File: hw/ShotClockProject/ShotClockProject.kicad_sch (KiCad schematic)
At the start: 8 parts, among them SW1 PS-5824SVB-6PL

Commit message: Finshed both schematics
- LED driving transistors are placed
- All connectors on segment display PCB are placed
- All schematic references have been re-configured (autosort on Y axis)
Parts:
- renumbered R39 to R3, R40 to R4, TP2 to TP1, TP1 to TP2, TP12 to TP3
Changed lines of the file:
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@@
   (symbol (lib_id "Connector:TestPoint") (at 144.78 54.61 0) (mirror y) (unit 1)
     (in_bom yes) (on_board yes) (dnp no)
-    (property "Reference" "TP12" (at 143.51 49.53 0)
+    (property "Reference" "TP3" (at 143.51 49.53 0)
       (effects (font (size 1.27 1.27)) (justify left))
     )
@@
       (project "ShotClockProject"
         (path "/5fd859aa-754d-49c2-9762-3f7ebe3bb64c"
-          (reference "TP12") (unit 1)
+          (reference "TP3") (unit 1)
         )
         (path "/5fd859aa-754d-49c2-9762-3f7ebe3bb64c/17367eb9-0f4d-4017-b1ca-d50430410a5d"
@@
         )
         (path "/5fd859aa-754d-49c2-9762-3f7ebe3bb64c"
-          (reference "#FLG013") (unit 1)
+          (reference "#FLG02") (unit 1)
         )
       )
@@
   (symbol (lib_id "Connector:TestPoint") (at 144.78 35.56 0) (mirror y) (unit 1)
     (in_bom yes) (on_board yes) (dnp no)
-    (property "Reference" "TP2" (at 143.51 30.48 0)
+    (property "Reference" "TP1" (at 143.51 30.48 0)
       (effects (font (size 1.27 1.27)) (justify left))
     )
@@
       (project "ShotClockProject"
         (path "/5fd859aa-754d-49c2-9762-3f7ebe3bb64c"
-          (reference "TP2") (unit 1)
+          (reference "TP1") (unit 1)
         )
         (path "/5fd859aa-754d-49c2-9762-3f7ebe3bb64c/17367eb9-0f4d-4017-b1ca-d50430410a5d"
@@
   (symbol (lib_id "power:+5V") (at 160.02 53.34 0) (unit 1)
     (in_bom yes) (on_board yes) (dnp no) (fields_autoplaced)
-    (property "Reference" "#PWR089" (at 160.02 57.15 0)
+    (property "Reference" "#PWR02" (at 160.02 57.15 0)
       (effects (font (size 1.27 1.27)) hide)
     )
@@
       (project "ShotClockProject"
         (path "/5fd859aa-754d-49c2-9762-3f7ebe3bb64c"
-          (reference "#PWR089") (unit 1)
+          (reference "#PWR02") (unit 1)
         )
       )
@@
   (symbol (lib_id "Device:R") (at 149.86 54.61 90) (unit 1)
     (in_bom yes) (on_board yes) (dnp no) (fields_autoplaced)
-    (property "Reference" "R40" (at 149.86 48.26 90)
+    (property "Reference" "R4" (at 149.86 48.26 90)
       (effects (font (size 1.27 1.27)))
     )
@@
       (project "ShotClockProject"
         (path "/5fd859aa-754d-49c2-9762-3f7ebe3bb64c"
-          (reference "R40") (unit 1)
+          (reference "R4") (unit 1)
         )
       )
@@
   (symbol (lib_id "Connector:TestPoint") (at 59.69 49.53 0) (mirror y) (unit 1)
     (in_bom yes) (on_board yes) (dnp no)
-    (property "Reference" "TP1" (at 58.42 45.72 0)
+    (property "Reference" "TP2" (at 58.42 45.72 0)
       (effects (font (size 1.27 1.27)) (justify left))
     )
@@
       (project "ShotClockProject"
         (path "/5fd859aa-754d-49c2-9762-3f7ebe3bb64c"
-          (reference "TP1") (unit 1)
+          (reference "TP2") (unit 1)
         )
         (path "/5fd859aa-754d-49c2-9762-3f7ebe3bb64c/d287d155-1951-4d4f-8d6c-570f03bc79f5"
@@
   (symbol (lib_id "Device:R") (at 101.6 54.61 90) (unit 1)
     (in_bom yes) (on_board yes) (dnp no) (fields_autoplaced)
-    (property "Reference" "R39" (at 101.6 48.26 90)
+    (property "Reference" "R3" (at 101.6 48.26 90)
       (effects (font (size 1.27 1.27)))
     )
@@
       (project "ShotClockProject"
         (path "/5fd859aa-754d-49c2-9762-3f7ebe3bb64c"
-          (reference "R39") (unit 1)
-        )
-      )
+          (reference "R3") (unit 1)
+        )
+      )

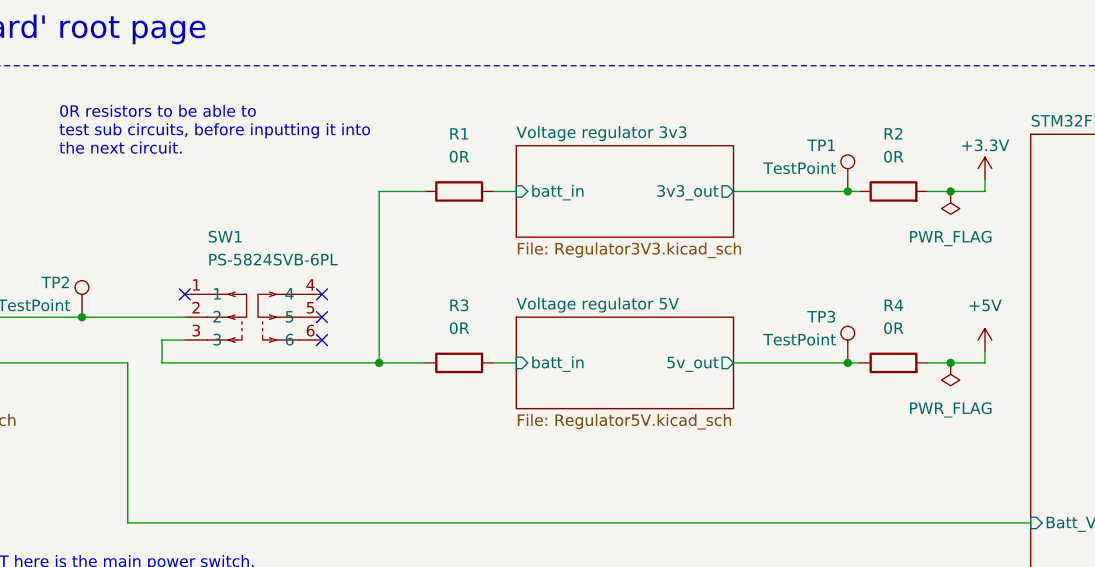
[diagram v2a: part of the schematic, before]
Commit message: Redid layout with new board dimensions
Changed tactile switches to larger push switches (also momentary)
Changed USART1 to UART4 & added UART5 to STDC14 connector
Placed all components nearer to each other, and within the PCB outer edge
Added rounded corners
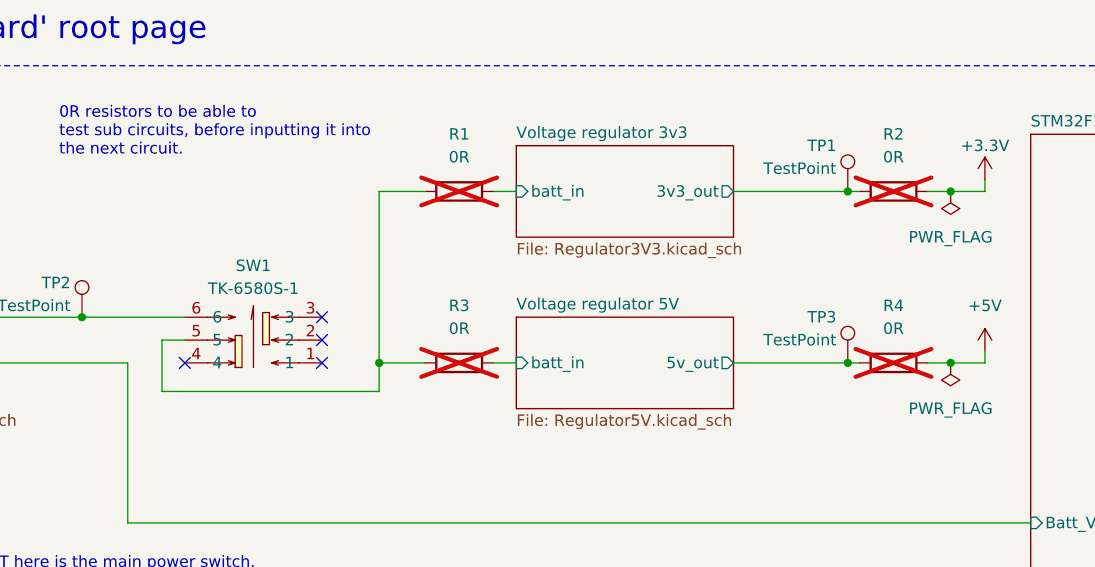
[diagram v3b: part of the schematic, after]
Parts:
- removed SW1: PS-5824SVB-6PL, PS-5824SVB-6PL:SW-SMD_6P-L5.8-W5.8-P2.00-LS11.3, symbol PS-5824SVB-6PL:PS-5824SVB-6PL
- added SW1: TK-6580S-1, TK-6580S-1:SW-SMD_TK-6580S-1, symbol TK-6580S-1:TK-6580S-1
- R1, R2, R3, R4: now not fitted
- TP1, TP2, TP3: footprint TestPoint:TestPoint_Pad_D2.5mm -> TestPoint:TestPoint_Pad_D1.0mm
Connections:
- net Li-Po Battery and charger/charger_out: now also SW1.6
- net at R1.1, R3.1: now also SW1.5

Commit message: Routed almost everything, except display connector
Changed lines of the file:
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@@
   (no_connect (at 86.36 52.07))
   (no_connect (at 86.36 49.53))
+  (bus_entry (at 118.745 120.015) (size 2.54 2.54)
+    (stroke (width 0) (type default))
+  )
   (wire (pts (xy 203.2 45.72) (xy 231.14 45.72))
     (stroke (width 0) (type default))

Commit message: Added LCSC Part number
Renamed output folders
Created first output files for REV1
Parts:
- R1, R2, R3, R4: LCSC Part (none) -> C17168; LCSC Part # (none) -> C17168
- SW1: LCSC Part # (none) -> C528774
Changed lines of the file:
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@@
       (effects (font (size 1.27 1.27)) hide)
     )
-    (property "LCSC Part" "C528774" (at 96.52 52.07 0)
+    (property "LCSC Part #" "C528774" (at 78.74 52.07 0)
+      (effects (font (size 1.27 1.27)) hide)
+    )
+    (property "LCSC Part" "C528774" (at 78.74 52.07 0)
       (effects (font (size 1.27 1.27)) hide)
     )
@@
       (effects (font (size 1.27 1.27)) hide)
     )
+    (property "LCSC Part #" "" (at 144.78 54.61 0)
+      (effects (font (size 1.27 1.27)) hide)
+    )
+    (property "LCSC Part" "" (at 144.78 54.61 0)
+      (effects (font (size 1.27 1.27)) hide)
+    )
     (pin "1")
     (instances
@@
       (effects (font (size 1.27 1.27)) hide)
     )
+    (property "LCSC Part #" "" (at 144.78 35.56 0)
+      (effects (font (size 1.27 1.27)) hide)
+    )
+    (property "LCSC Part" "" (at 144.78 35.56 0)
+      (effects (font (size 1.27 1.27)) hide)
+    )
     (pin "1")
     (instances
@@
       (effects (font (size 1.27 1.27)) hide)
     )
+    (property "LCSC Part #" "C17168" (at 149.86 35.56 0)
+      (effects (font (size 1.27 1.27)) hide)
+    )
+    (property "LCSC Part" "C17168" (at 149.86 35.56 0)
+      (effects (font (size 1.27 1.27)) hide)
+    )
     (pin "1")
     (pin "2")
@@
       (effects (font (size 1.27 1.27)) hide)
     )
+    (property "LCSC Part #" "C17168" (at 101.6 35.56 0)
+      (effects (font (size 1.27 1.27)) hide)
+    )
+    (property "LCSC Part" "C17168" (at 101.6 35.56 0)
+      (effects (font (size 1.27 1.27)) hide)
+    )
     (pin "1")
     (pin "2")
@@
       (effects (font (size 1.27 1.27)) hide)
     )
+    (property "LCSC Part #" "C17168" (at 149.86 54.61 0)
+      (effects (font (size 1.27 1.27)) hide)
+    )
+    (property "LCSC Part" "C17168" (at 149.86 54.61 0)
+      (effects (font (size 1.27 1.27)) hide)
+    )
     (pin "1")
     (pin "2")
@@
       (effects (font (size 1.27 1.27)) hide)
     )
+    (property "LCSC Part #" "" (at 59.69 49.53 0)
+      (effects (font (size 1.27 1.27)) hide)
+    )
+    (property "LCSC Part" "" (at 59.69 49.53 0)
+      (effects (font (size 1.27 1.27)) hide)
+    )
     (pin "1")
     (instances
@@
       (effects (font (size 1.27 1.27)) hide)
     )
+    (property "LCSC Part #" "C17168" (at 101.6 54.61 0)
+      (effects (font (size 1.27 1.27)) hide)
+    )
+    (property "LCSC Part" "C17168" (at 101.6 54.61 0)
+      (effects (font (size 1.27 1.27)) hide)
+    )

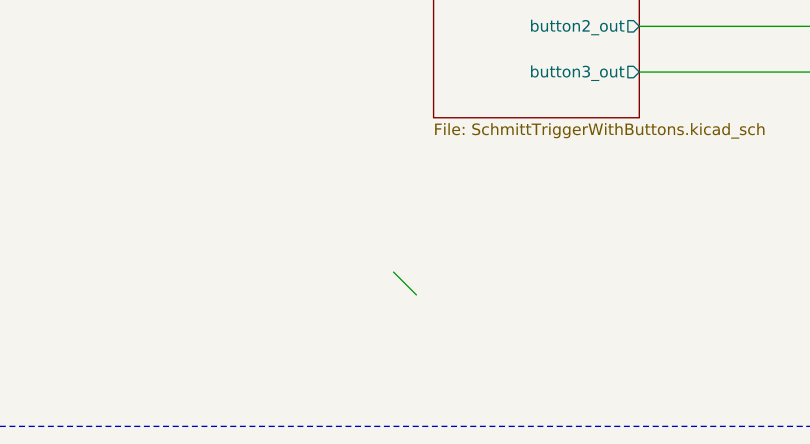
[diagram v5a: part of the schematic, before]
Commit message: Added LCSC part numbers, and changed TPS vias
- Changed the footprint for the TPS regulators, so they don't have 0.2mm vias. Manually placed GND vias next to the footprint.
- Removed NETTIES to get rid of weird across the map connection of GND and GNDPWR.
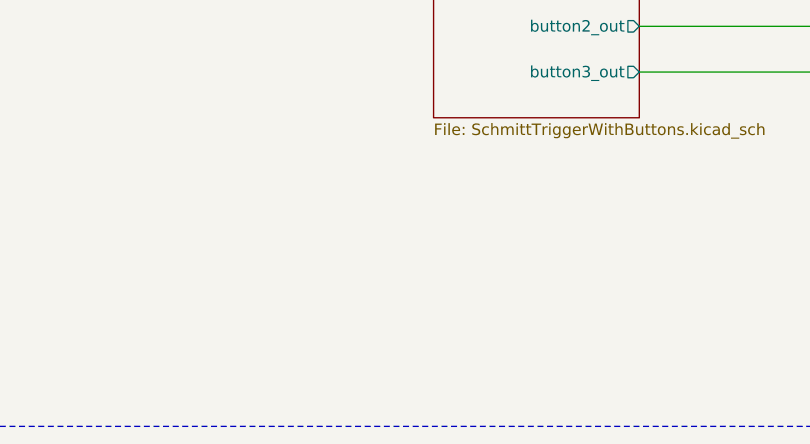
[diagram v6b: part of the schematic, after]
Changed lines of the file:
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@@
   (no_connect (at 86.36 52.07))
   (no_connect (at 86.36 49.53))
-  (bus_entry (at 118.745 120.015) (size 2.54 2.54)
-    (stroke (width 0) (type default))
-  )
   (wire (pts (xy 203.2 45.72) (xy 231.14 45.72))
     (stroke (width 0) (type default))

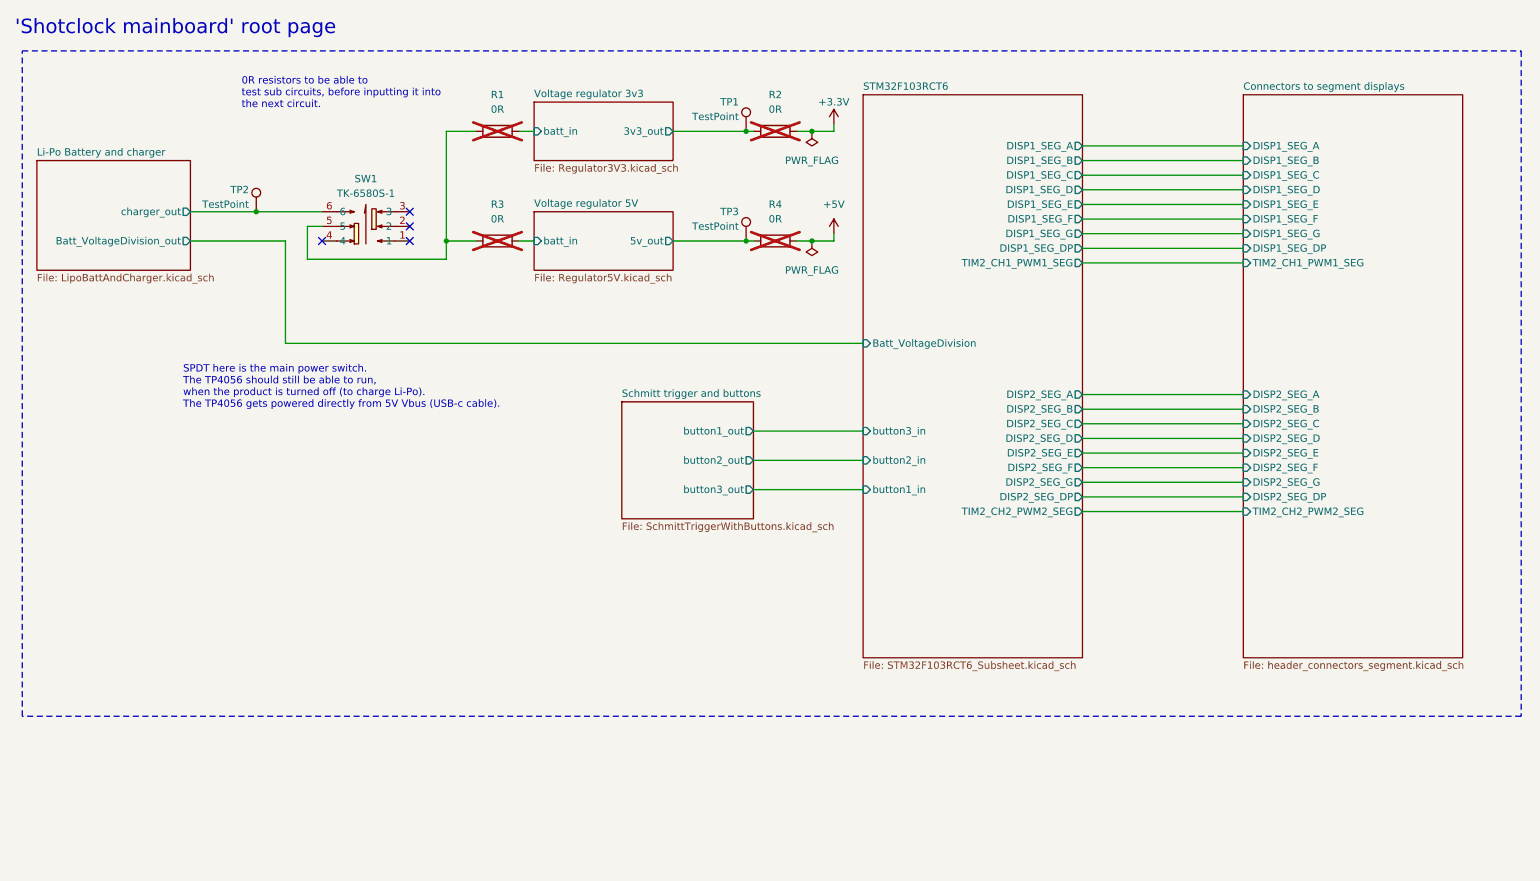
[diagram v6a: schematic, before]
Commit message: Started on integrating new STM32 MCU
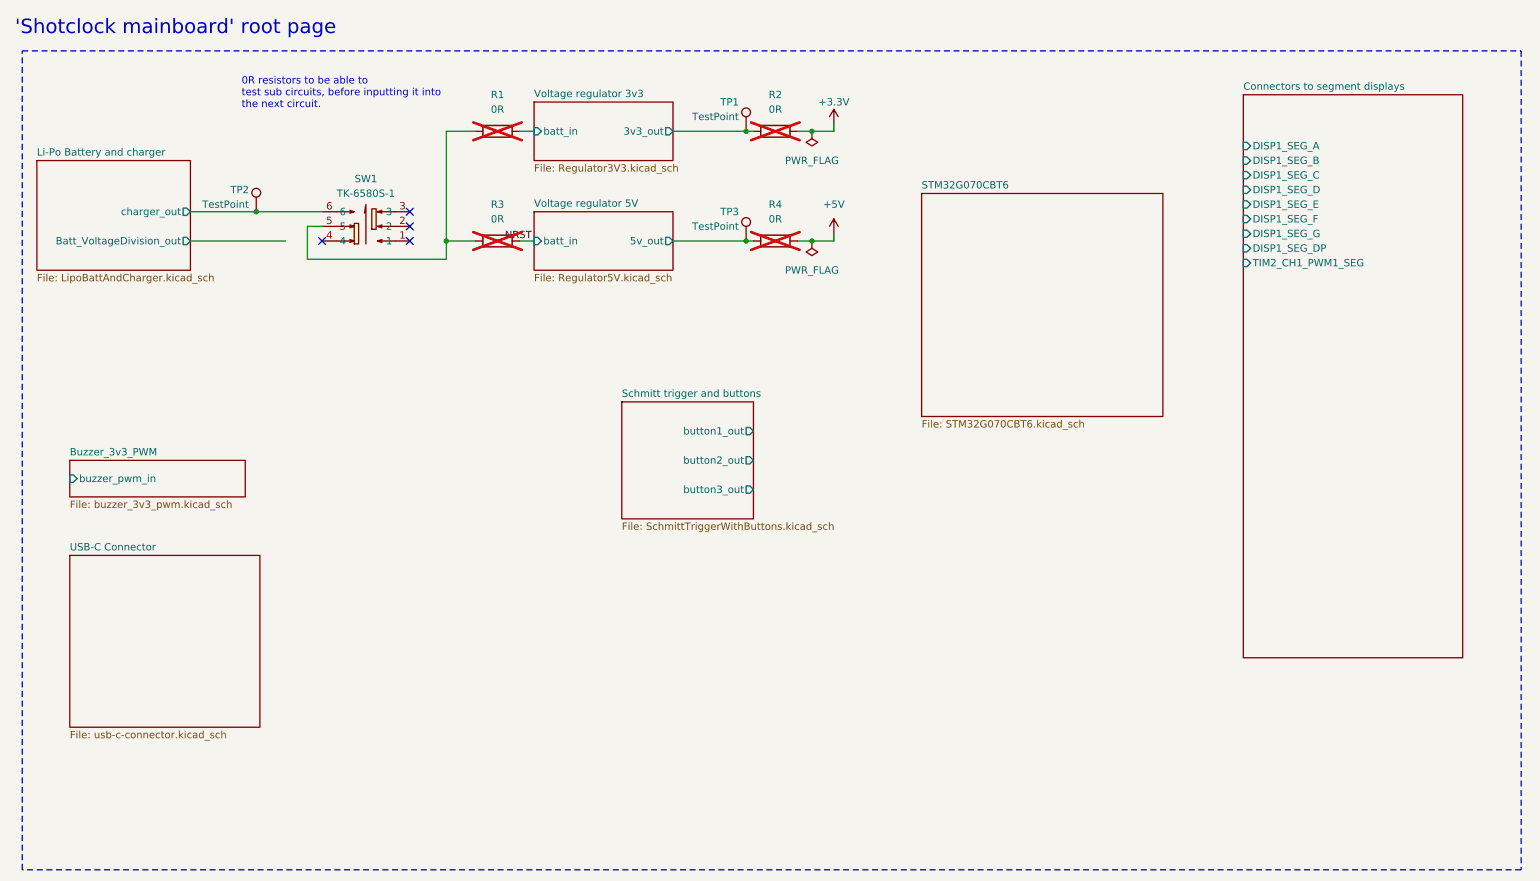
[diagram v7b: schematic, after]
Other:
- removed sheet STM32F103RCT6
- added sheet Buzzer_3v3_PWM (buzzer_3v3_pwm.kicad_sch)
- added sheet STM32G070CBT6 (STM32G070CBT6.kicad_sch)
- added sheet USB-C Connector (usb-c-connector.kicad_sch)
- sheet Connectors to segment displays ports: added none; removed DISP2_SEG_A, DISP2_SEG_B, DISP2_SEG_C, DISP2_SEG_D, DISP2_SEG_DP, DISP2_SEG_E, DISP2_SEG_F, DISP2_SEG_G, TIM2_CH2_PWM2_SEG
- note removed: "SPDT here is the main power switch. The TP4056 should still be able to run, when the product is turned off (to charge Li-Po). The TP4056 gets powered directly from 5V Vbus (USB-c cable)."
